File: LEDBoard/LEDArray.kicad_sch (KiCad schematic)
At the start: 110 parts

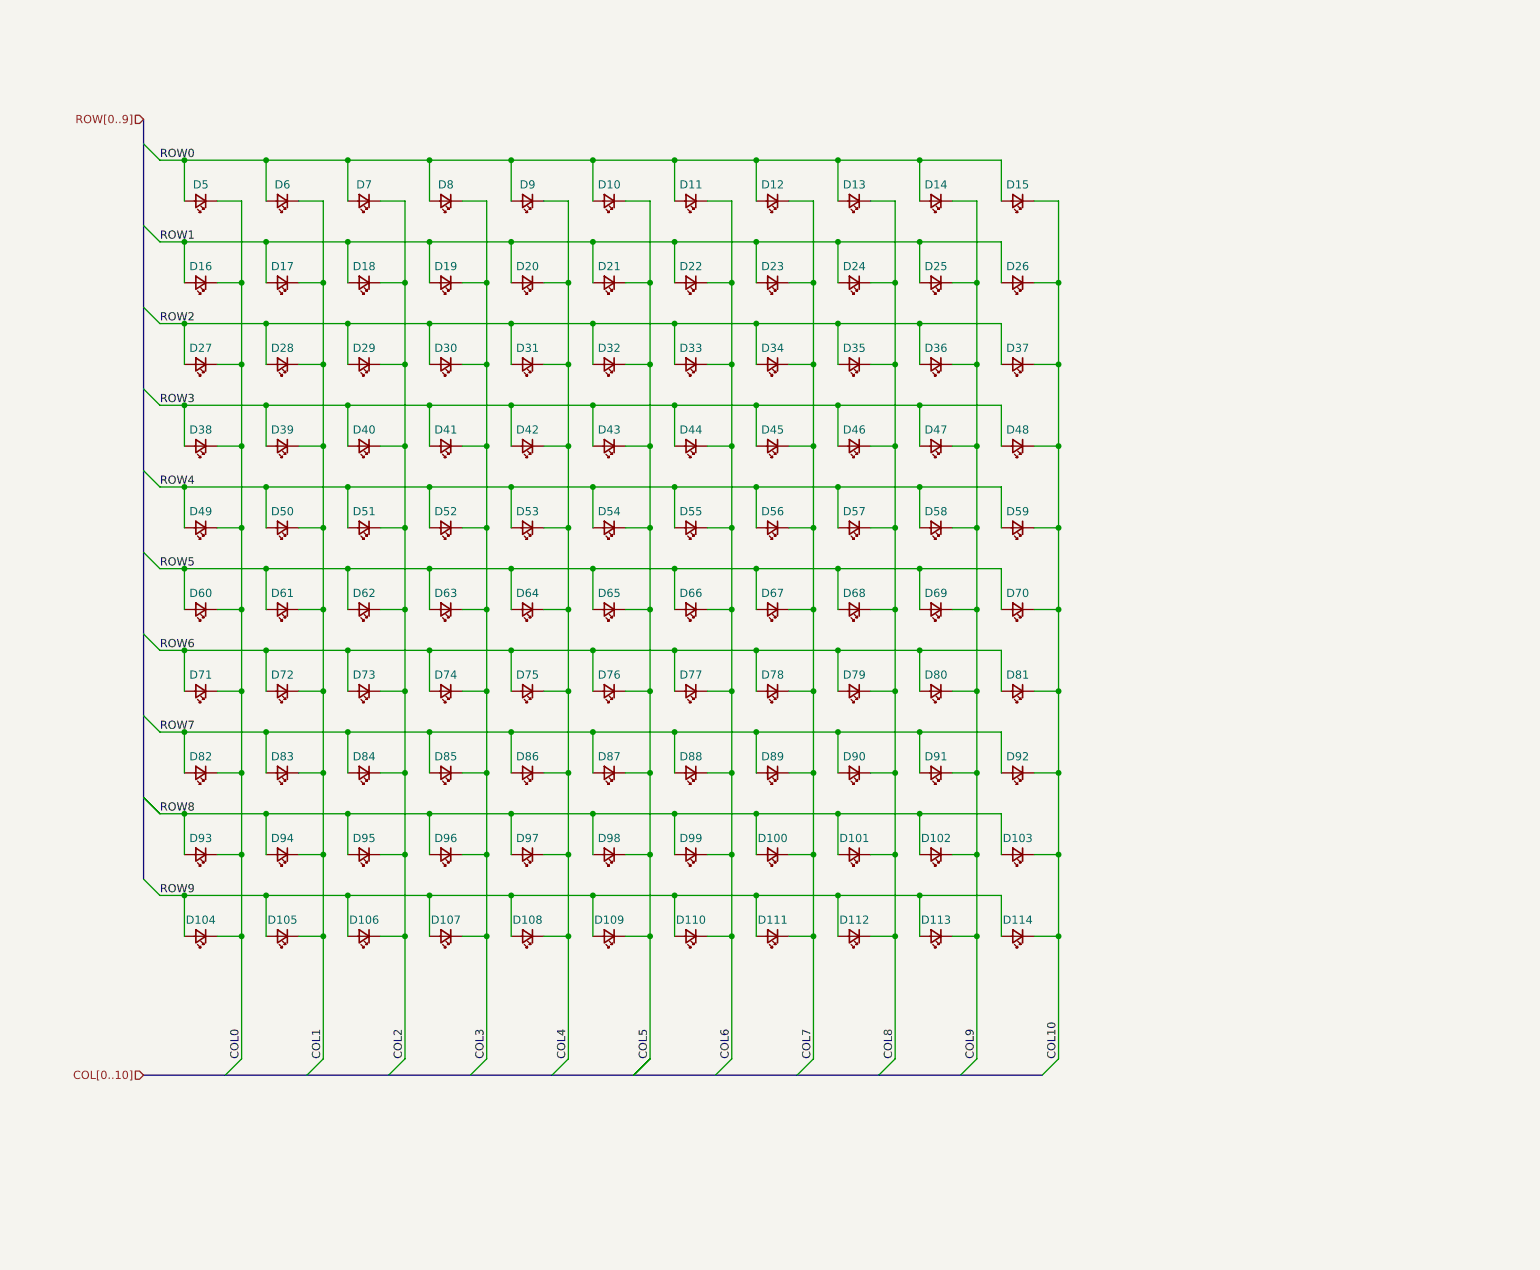
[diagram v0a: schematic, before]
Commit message: Change led matrix routing for sinking current through mcu, sourcing from battery
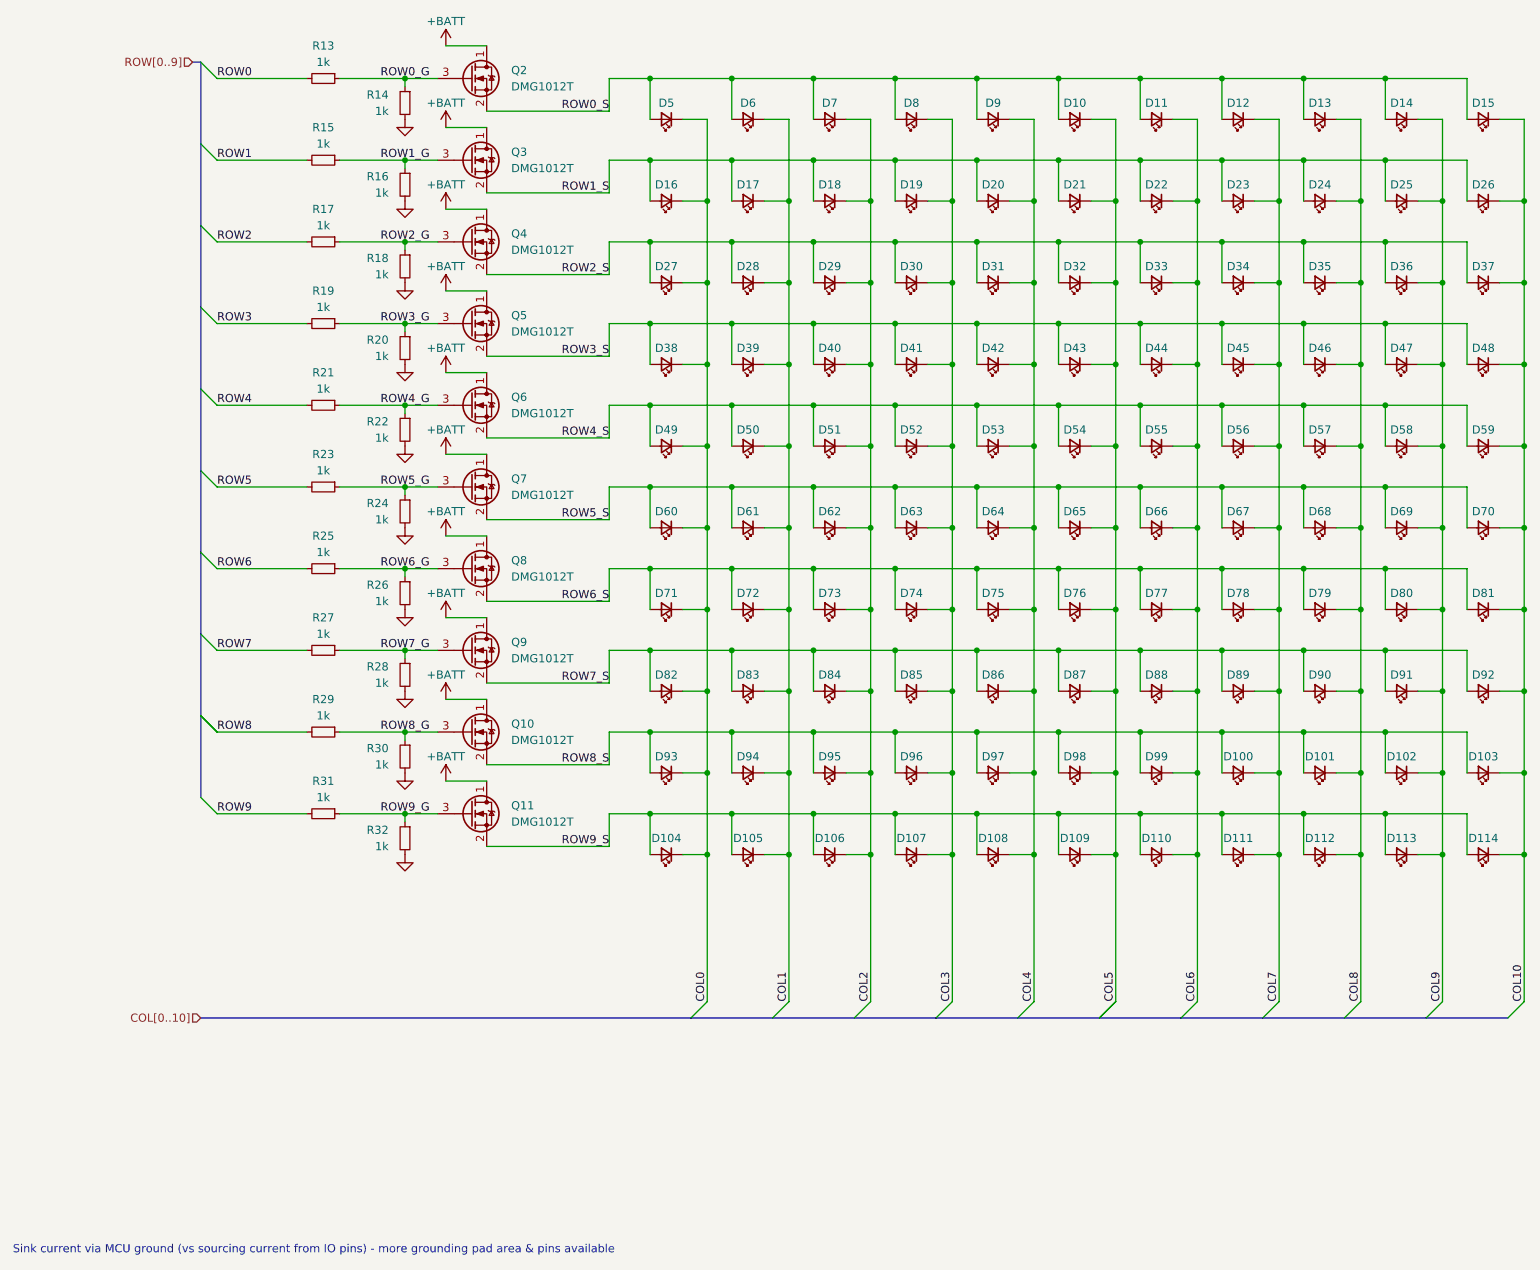
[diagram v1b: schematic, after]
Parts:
- added Q10, Q11, Q2, Q3, Q4, Q5, Q6, Q7, Q8, Q9: DMG1012T, Package_TO_SOT_SMD:SOT-523, symbol Device:Q_NMOS_DSG
- added R13, R14, R15, R16, R17, R18, R19, R20, R21, R22, R23, R24, R25, R26, R27, R28, R29, R30, R31, R32: 1k, Resistor_SMD:R_0402_1005Metric, symbol Device:R_Small
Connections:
- net ROW0: now also R13.2; no longer D10.2 (A), D11.2 (A), D12.2 (A), D13.2 (A), D14.2 (A), D15.2 (A), D5.2 (A), D6.2 (A), D7.2 (A), D8.2 (A), D9.2 (A)
- net ROW1: now also R15.2; no longer D16.2 (A), D17.2 (A), D18.2 (A), D19.2 (A), D20.2 (A), D21.2 (A), D22.2 (A), D23.2 (A), D24.2 (A), D25.2 (A), D26.2 (A)
- net ROW2: now also R17.2; no longer D27.2 (A), D28.2 (A), D29.2 (A), D30.2 (A), D31.2 (A), D32.2 (A), D33.2 (A), D34.2 (A), D35.2 (A), D36.2 (A), D37.2 (A)
- net ROW3: now also R19.2; no longer D38.2 (A), D39.2 (A), D40.2 (A), D41.2 (A), D42.2 (A), D43.2 (A), D44.2 (A), D45.2 (A), D46.2 (A), D47.2 (A), D48.2 (A)
- net ROW4: now also R21.2; no longer D49.2 (A), D50.2 (A), D51.2 (A), D52.2 (A), D53.2 (A), D54.2 (A), D55.2 (A), D56.2 (A), D57.2 (A), D58.2 (A), D59.2 (A)
- net ROW5: now also R23.2; no longer D60.2 (A), D61.2 (A), D62.2 (A), D63.2 (A), D64.2 (A), D65.2 (A), D66.2 (A), D67.2 (A), D68.2 (A), D69.2 (A), D70.2 (A)
- net ROW6: now also R25.2; no longer D71.2 (A), D72.2 (A), D73.2 (A), D74.2 (A), D75.2 (A), D76.2 (A), D77.2 (A), D78.2 (A), D79.2 (A), D80.2 (A), D81.2 (A)
- net ROW7: now also R27.2; no longer D82.2 (A), D83.2 (A), D84.2 (A), D85.2 (A), D86.2 (A), D87.2 (A), D88.2 (A), D89.2 (A), D90.2 (A), D91.2 (A), D92.2 (A)
- net ROW8: now also R29.2; no longer D100.2 (A), D101.2 (A), D102.2 (A), D103.2 (A), D93.2 (A), D94.2 (A), D95.2 (A), D96.2 (A), D97.2 (A), D98.2 (A), D99.2 (A)
- net ROW9: now also R31.2; no longer D104.2 (A), D105.2 (A), D106.2 (A), D107.2 (A), D108.2 (A), D109.2 (A), D110.2 (A), D111.2 (A), D112.2 (A), D113.2 (A), D114.2 (A)
- new net +BATT: Q10.1 (D), Q11.1 (D), Q2.1 (D), Q3.1 (D), Q4.1 (D), Q5.1 (D), Q6.1 (D), Q7.1 (D), Q8.1 (D), Q9.1 (D)
- new net GND: R14.2, R16.2, R18.2, R20.2, R22.2, R24.2, R26.2, R28.2, R30.2, R32.2
- new net ROW0_G: Q2.3 (G), R13.1, R14.1
- new net ROW0_S: D10.2 (A), D11.2 (A), D12.2 (A), D13.2 (A), D14.2 (A), D15.2 (A), D5.2 (A), D6.2 (A), D7.2 (A), D8.2 (A), D9.2 (A), Q2.2 (S)
- new net ROW1_G: Q3.3 (G), R15.1, R16.1
- new net ROW1_S: D16.2 (A), D17.2 (A), D18.2 (A), D19.2 (A), D20.2 (A), D21.2 (A), D22.2 (A), D23.2 (A), D24.2 (A), D25.2 (A), D26.2 (A), Q3.2 (S)
- new net ROW2_G: Q4.3 (G), R17.1, R18.1
- new net ROW2_S: D27.2 (A), D28.2 (A), D29.2 (A), D30.2 (A), D31.2 (A), D32.2 (A), D33.2 (A), D34.2 (A), D35.2 (A), D36.2 (A), D37.2 (A), Q4.2 (S)
- new net ROW3_G: Q5.3 (G), R19.1, R20.1
- new net ROW3_S: D38.2 (A), D39.2 (A), D40.2 (A), D41.2 (A), D42.2 (A), D43.2 (A), D44.2 (A), D45.2 (A), D46.2 (A), D47.2 (A), D48.2 (A), Q5.2 (S)
- new net ROW4_G: Q6.3 (G), R21.1, R22.1
- new net ROW4_S: D49.2 (A), D50.2 (A), D51.2 (A), D52.2 (A), D53.2 (A), D54.2 (A), D55.2 (A), D56.2 (A), D57.2 (A), D58.2 (A), D59.2 (A), Q6.2 (S)
- new net ROW5_G: Q7.3 (G), R23.1, R24.1
- new net ROW5_S: D60.2 (A), D61.2 (A), D62.2 (A), D63.2 (A), D64.2 (A), D65.2 (A), D66.2 (A), D67.2 (A), D68.2 (A), D69.2 (A), D70.2 (A), Q7.2 (S)
- new net ROW6_G: Q8.3 (G), R25.1, R26.1
- new net ROW6_S: D71.2 (A), D72.2 (A), D73.2 (A), D74.2 (A), D75.2 (A), D76.2 (A), D77.2 (A), D78.2 (A), D79.2 (A), D80.2 (A), D81.2 (A), Q8.2 (S)
- new net ROW7_G: Q9.3 (G), R27.1, R28.1
- new net ROW7_S: D82.2 (A), D83.2 (A), D84.2 (A), D85.2 (A), D86.2 (A), D87.2 (A), D88.2 (A), D89.2 (A), D90.2 (A), D91.2 (A), D92.2 (A), Q9.2 (S)
- new net ROW8_G: Q10.3 (G), R29.1, R30.1
- new net ROW8_S: D100.2 (A), D101.2 (A), D102.2 (A), D103.2 (A), D93.2 (A), D94.2 (A), D95.2 (A), D96.2 (A), D97.2 (A), D98.2 (A), D99.2 (A), Q10.2 (S)
- new net ROW9_G: Q11.3 (G), R31.1, R32.1
- new net ROW9_S: D104.2 (A), D105.2 (A), D106.2 (A), D107.2 (A), D108.2 (A), D109.2 (A), D110.2 (A), D111.2 (A), D112.2 (A), D113.2 (A), D114.2 (A), Q11.2 (S)
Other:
- note added: "Sink current via MCU ground (vs sourcing current from IO pins) - more grounding pad area & pins available"
- title: (none) -> WordWatch - LED Board
- moved on the sheet: D10, D100, D101, D102, D103, D104, D105, D106, D107, D108, D109, D11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
